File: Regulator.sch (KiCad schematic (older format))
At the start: 6 parts, among them U2 MIC29303WU

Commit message: fixed pcb layout
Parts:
- R5: footprint Resistor_SMD:R_0805_2012Metric_Pad1.20x1.40mm_HandSolder -> Resistor_SMD:R_0805_2012Metric_Pad1.15x1.40mm_HandSolder
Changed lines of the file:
@@
 F 0 "R5" H 7120 4296 50  0000 L CNN
 F 1 "18" H 7120 4205 50  0000 L CNN
-F 2 "Resistor_SMD:R_0805_2012Metric_Pad1.20x1.40mm_HandSolder" V 6980 4250 50  0001 C CNN
+F 2 "Resistor_SMD:R_0805_2012Metric_Pad1.15x1.40mm_HandSolder" V 6980 4250 50  0001 C CNN
 F 3 "~" H 7050 4250 50  0001 C CNN
 	1    7050 4250

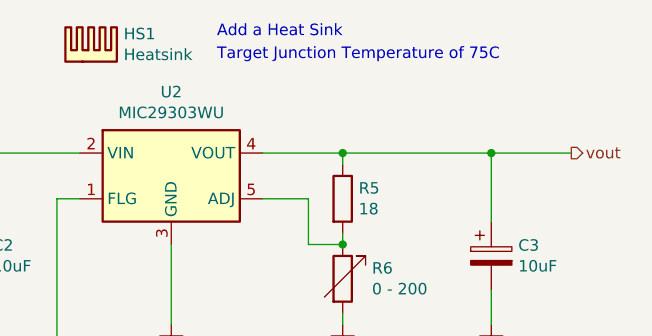
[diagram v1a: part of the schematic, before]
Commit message: added new heatsink alterantive
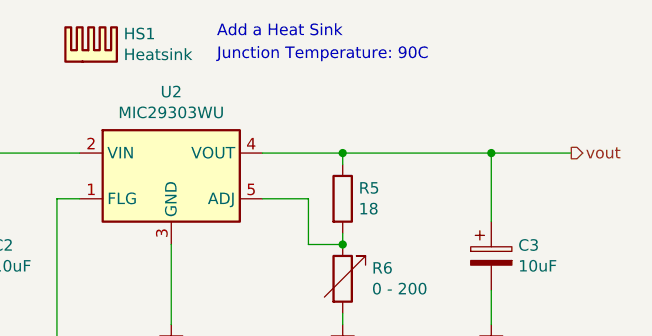
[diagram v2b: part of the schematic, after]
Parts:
- C2, C3: footprint Capacitor_Tantalum_SMD:CP_EIA-3216-12_Kemet-S_Pad1.58x1.35mm_HandSolder -> Capacitor_SMD:C_0805_2012Metric_Pad1.18x1.45mm_HandSolder; dk_pn (none) -> 1276-2891-1-ND
- HS1: footprint Heatsink:547-95AB -> heatsink-lib:ATS-1139-C1-R0
- R5: dk_pn (none) -> P100KDACT-ND; ms_pn (none) -> 667-ERA-6AHD180V
- R6: footprint Potentiometer_SMD:Potentiometer_Bourns_TC33X_Vertical -> Potentiometer_SMD:Potentiometer_Bourns_3224G_Horizontal; dk_pn (none) -> 3224G-1-201ECT-ND; ms_pn (none) -> 652-3224G-1-201E
- U2: dk_pn (none) -> MIC29303WU-CT-ND; ms_pn (none) -> 998-MIC29303WU
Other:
- note added: "Junction Temperature: 90C"
- note removed: "Target Junction Temperature of 75C"
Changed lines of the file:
@@
 F 2 "Resistor_SMD:R_0805_2012Metric_Pad1.15x1.40mm_HandSolder" V 6980 4250 50  0001 C CNN
 F 3 "~" H 7050 4250 50  0001 C CNN
+F 4 "667-ERA-6AHD180V" H 7050 4250 50  0001 C CNN "ms_pn"
+F 5 "P100KDACT-ND" H 7050 4250 50  0001 C CNN "dk_pn"
 	1    7050 4250
 	1    0    0    -1
@@
 F 0 "C2" H 5518 4546 50  0000 L CNN
 F 1 "10uF" H 5518 4455 50  0000 L CNN
-F 2 "Capacitor_Tantalum_SMD:CP_EIA-3216-12_Kemet-S_Pad1.58x1.35mm_HandSolder" H 5438 4350 50  0001 C CNN
+F 2 "Capacitor_SMD:C_0805_2012Metric_Pad1.18x1.45mm_HandSolder" H 5438 4350 50  0001 C CNN
 F 3 "~" H 5400 4500 50  0001 C CNN
+F 4 "" H 5400 4500 50  0001 C CNN "ms_pn"
+F 5 "1276-2891-1-ND" H 5400 4500 50  0001 C CNN "dk_pn"
 	1    5400 4500
 	1    0    0    -1
@@
 F 0 "R6" H 7178 4646 50  0000 L CNN
 F 1 "0 - 200" H 7178 4555 50  0000 L CNN
-F 2 "Potentiometer_SMD:Potentiometer_Bourns_TC33X_Vertical" V 6980 4600 50  0001 C CNN
+F 2 "Potentiometer_SMD:Potentiometer_Bourns_3224G_Horizontal" V 6980 4600 50  0001 C CNN
 F 3 "~" H 7050 4600 50  0001 C CNN
+F 4 "652-3224G-1-201E" H 7050 4600 50  0001 C CNN "ms_pn"
+F 5 "3224G-1-201ECT-ND" H 7050 4600 50  0001 C CNN "dk_pn"
 	1    7050 4600
 	1    0    0    -1
@@
 F 2 "Package_TO_SOT_SMD:TO-263-5_TabPin3" H 6400 3900 50  0001 L CNN
 F 3 "http://ww1.microchip.com/downloads/en/devicedoc/20005685a.pdf" H 6300 4150 50  0001 C CNN
+F 4 "998-MIC29303WU" H 6300 4150 50  0001 C CNN "ms_pn"
+F 5 "MIC29303WU-CT-ND" H 6300 4150 50  0001 C CNN "dk_pn"
 	1    6300 4150
 	1    0    0    -1
@@
 Add a Heat Sink
 Text Notes 6500 3650 0    50   ~ 0
-Target Junction Temperature of 75C
+Junction Temperature: 90C
 $Comp
 L Device:CP C?
@@
 F 0 "C3" H 7818 4546 50  0000 L CNN
 F 1 "10uF" H 7818 4455 50  0000 L CNN
-F 2 "Capacitor_Tantalum_SMD:CP_EIA-3216-12_Kemet-S_Pad1.58x1.35mm_HandSolder" H 7738 4350 50  0001 C CNN
+F 2 "Capacitor_SMD:C_0805_2012Metric_Pad1.18x1.45mm_HandSolder" H 7738 4350 50  0001 C CNN
 F 3 "~" H 7700 4500 50  0001 C CNN
+F 4 "" H 7700 4500 50  0001 C CNN "ms_pn"
+F 5 "1276-2891-1-ND" H 7700 4500 50  0001 C CNN "dk_pn"
 	1    7700 4500
 	1    0    0    -1
@@
 F 0 "HS1" H 6092 3771 50  0000 L CNN
 F 1 "Heatsink" H 6092 3680 50  0000 L CNN
-F 2 "Heatsink:547-95AB" H 5962 3650 50  0001 C CNN
+F 2 "heatsink-lib:ATS-1139-C1-R0" H 5962 3650 50  0001 C CNN
 F 3 "~" H 5962 3650 50  0001 C CNN
+F 4 "" H 5950 3650 50  0001 C CNN "ms_pn"
 	1    5950 3650
 	1    0    0    -1

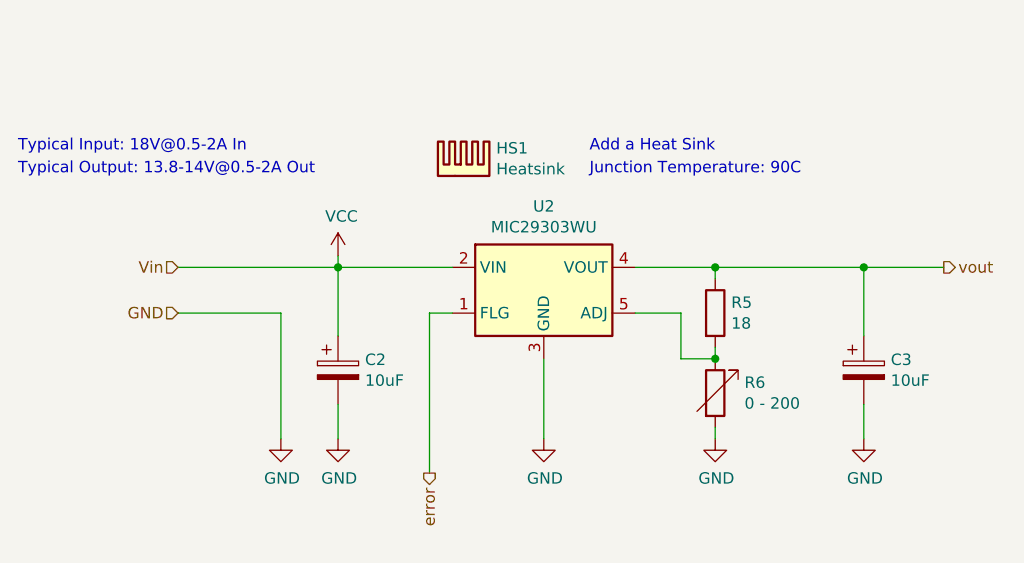
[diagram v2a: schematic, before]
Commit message: changed layout for heat sink w/ issue #1
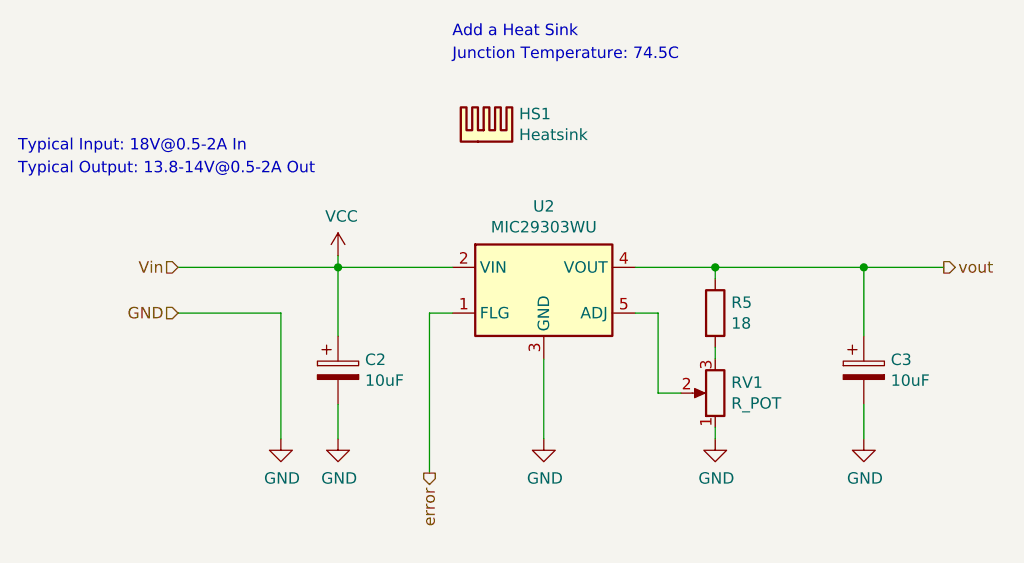
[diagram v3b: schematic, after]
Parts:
- removed R6: 0 - 200, Potentiometer_SMD:Potentiometer_Bourns_3224G_Horizontal, symbol Device:R_Variable
- added RV1: R_POT, potentiometer-lib:TC33X-2-201G, symbol Device:R_POT
- C2, C3: ms_pn (none) -> 187-CL21A106KAYNNNE
- HS1: footprint heatsink-lib:ATS-1139-C1-R0 -> heatsink-lib:Ohmite-BGAH450125E; dk_pn (none) -> 273-BGAH450-125E-ND; ms_pn (none) -> 588-BGAH450-125E
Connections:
- net GND: now also RV1.1
- net at R5.2: now also RV1.3; no longer U2.5 (ADJ)
- new net: RV1.2, U2.5 (ADJ)
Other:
- note added: "Junction Temperature: 74.5C"
- note removed: "Junction Temperature: 90C"
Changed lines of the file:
@@
 F 2 "Capacitor_SMD:C_0805_2012Metric_Pad1.18x1.45mm_HandSolder" H 5438 4350 50  0001 C CNN
 F 3 "~" H 5400 4500 50  0001 C CNN
-F 4 "" H 5400 4500 50  0001 C CNN "ms_pn"
+F 4 "187-CL21A106KAYNNNE" H 5400 4500 50  0001 C CNN "ms_pn"
 F 5 "1276-2891-1-ND" H 5400 4500 50  0001 C CNN "dk_pn"
 	1    5400 4500
@@
 	5400 4000 5400 4050
 $Comp
-L Device:R_Variable R?
-U 1 1 602A55F6
-P 7050 4600
-AR Path="/602A55F6" Ref="R?"  Part="1"
-AR Path="/602A1165/602A55F6" Ref="R6"  Part="1"
-F 0 "R6" H 7178 4646 50  0000 L CNN
-F 1 "0 - 200" H 7178 4555 50  0000 L CNN
-F 2 "Potentiometer_SMD:Potentiometer_Bourns_3224G_Horizontal" V 6980 4600 50  0001 C CNN
-F 3 "~" H 7050 4600 50  0001 C CNN
-F 4 "652-3224G-1-201E" H 7050 4600 50  0001 C CNN "ms_pn"
-F 5 "3224G-1-201ECT-ND" H 7050 4600 50  0001 C CNN "dk_pn"
-	1    7050 4600
-	1    0    0    -1
-$EndComp
-$Comp
 L Regulator_Linear:MIC29303WU U?
 U 1 1 602A55FC
@@
 	7050 4400 7050 4450
 Wire Wire Line
-	6700 4250 6900 4250
-Wire Wire Line
-	6900 4250 6900 4450
-Wire Wire Line
-	6900 4450 7050 4450
-Connection ~ 7050 4450
-Text Notes 6500 3550 0    50   ~ 0
+	6700 4250 6800 4250
+Text Notes 5900 3050 0    50   ~ 0
 Add a Heat Sink
-Text Notes 6500 3650 0    50   ~ 0
-Junction Temperature: 90C
+Text Notes 5900 3150 0    50   ~ 0
+Junction Temperature: 74.5C
 $Comp
 L Device:CP C?
@@
 F 2 "Capacitor_SMD:C_0805_2012Metric_Pad1.18x1.45mm_HandSolder" H 7738 4350 50  0001 C CNN
 F 3 "~" H 7700 4500 50  0001 C CNN
-F 4 "" H 7700 4500 50  0001 C CNN "ms_pn"
+F 4 "187-CL21A106KAYNNNE" H 7700 4500 50  0001 C CNN "ms_pn"
 F 5 "1276-2891-1-ND" H 7700 4500 50  0001 C CNN "dk_pn"
 	1    7700 4500
@@
 $Comp
 L Mechanical:Heatsink HS1
-U 1 1 6030E825
-P 5950 3650
-F 0 "HS1" H 6092 3771 50  0000 L CNN
-F 1 "Heatsink" H 6092 3680 50  0000 L CNN
-F 2 "heatsink-lib:ATS-1139-C1-R0" H 5962 3650 50  0001 C CNN
-F 3 "~" H 5962 3650 50  0001 C CNN
-F 4 "" H 5950 3650 50  0001 C CNN "ms_pn"
-	1    5950 3650
+U 1 1 603BE6AA
+P 6050 3500
+F 0 "HS1" H 6192 3621 50  0000 L CNN
+F 1 "Heatsink" H 6192 3530 50  0000 L CNN
+F 2 "heatsink-lib:Ohmite-BGAH450125E" H 6062 3500 50  0001 C CNN
+F 3 "~" H 6062 3500 50  0001 C CNN
+F 4 "273-BGAH450-125E-ND" H 6050 3500 50  0001 C CNN "dk_pn"
+F 5 "588-BGAH450-125E" H 6050 3500 50  0001 C CNN "ms_pn"
+	1    6050 3500
 	1    0    0    -1
 $EndComp
+$Comp
+L Device:R_POT RV1
+U 1 1 603A579E
+P 7050 4600
+F 0 "RV1" H 6980 4554 50  0000 R CNN
+F 1 "R_POT" H 6980 4645 50  0000 R CNN
+F 2 "potentiometer-lib:TC33X-2-201G" H 7050 4600 50  0001 C CNN
+F 3 "~" H 7050 4600 50  0001 C CNN
+F 4 "TC33X-2-201G-ND" H 7050 4600 50  0001 C CNN "dk_pn"
+F 5 "652-TC33X-2-201G" H 7050 4600 50  0001 C CNN "ms_pn"
+	1    7050 4600
+	-1   0    0    1
+$EndComp
+Wire Wire Line
+	6900 4600 6800 4600
+Wire Wire Line
+	6800 4250 6800 4600
 $EndSCHEMATC
